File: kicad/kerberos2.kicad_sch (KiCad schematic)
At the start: 12 parts, among them J1 USB4125-GF-A_REVA2, J2 MIDI-in, J3 MIDI-thru, J4 MIDI-out, SW1 TL1105JAF160Q, U1 RP2040, U2 W9812G6KH-6, U3 T8Q144, U4 MX25L25645G

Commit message: first complete test version for Kerberos 2
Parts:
- removed D1, D2: LED, LED_THT:LED_D3.0mm, symbol Device:LED
- removed J1: USB4125-GF-A_REVA2, usb-c:GCT_USB4125-GF-A_REVA2, symbol USB4125-GF-A_REVA2:USB4125-GF-A_REVA2
- removed J2: MIDI-in, midi:CUI_SD-50BV, symbol SD-50BV:SD-50BV
- removed J3: MIDI-thru, midi:CUI_SD-50BV, symbol SD-50BV:SD-50BV
- removed J4: MIDI-out, midi:CUI_SD-50BV, symbol SD-50BV:SD-50BV
- removed SW1: TL1105JAF160Q, reset-button:SW_TL1105JAF160Q, symbol TL1105JAF160Q:TL1105JAF160Q
- removed U1: RP2040, rp2040:QFN40P700X700X90-57N, symbol RP2040:RP2040
- removed U2: W9812G6KH-6, Package_SO:TSOP-II-54_22.2x10.16mm_P0.8mm, symbol Memory_RAM:W9812G6KH-6
- removed U3: T8Q144, Package_QFP:LQFP-144_20x20mm_P0.5mm, symbol T8Q144:T8Q144
- added C1: 100n, Capacitor_SMD:C_0805_2012Metric, symbol Device:C
- added D1, D2: D_Schottky, Diode_SMD:D_SMA, symbol Device:D_Schottky
- added D3, D4: ~, LED_THT:LED_D3.0mm, symbol Device:LED
- added FB1: FerriteBead, Inductor_SMD:L_0805_2012Metric, symbol Device:FerriteBead
- added JP2: host-mode-supply, Connector_PinHeader_2.54mm:PinHeader_1x02_P2.54mm_Vertical, symbol Jumper:Jumper_2_Open
- added JP3: 3.3V+, Connector_PinHeader_2.54mm:PinHeader_1x02_P2.54mm_Vertical, symbol Jumper:Jumper_2_Open
- added JP4: 3.3V, Connector_PinHeader_2.54mm:PinHeader_1x02_P2.54mm_Vertical, symbol Jumper:Jumper_2_Open
- added JP5: 3.3V-, Connector_PinHeader_2.54mm:PinHeader_1x02_P2.54mm_Vertical, symbol Jumper:Jumper_2_Open
- added JP6: 1.2V+, Connector_PinHeader_2.54mm:PinHeader_1x02_P2.54mm_Vertical, symbol Jumper:Jumper_2_Open
- added JP7: 1.2V, Connector_PinHeader_2.54mm:PinHeader_1x02_P2.54mm_Vertical, symbol Jumper:Jumper_2_Open
- added JP8: 1.2V-, Connector_PinHeader_2.54mm:PinHeader_1x02_P2.54mm_Vertical, symbol Jumper:Jumper_2_Open
- added R1, R2: 5.1, Resistor_SMD:R_0805_2012Metric, symbol Device:R
- added R10, R11, R12, R13, R14, R15, R16, R17, R18, R19, R7, R8, R9: 22, Resistor_SMD:R_0805_2012Metric, symbol Device:R
- added R20, R21: 1k, Resistor_SMD:R_0805_2012Metric, symbol Device:R
- added R3, R4, R5, R6: 27, Resistor_SMD:R_0805_2012Metric, symbol Device:R
- added RN1, RN2, RN3, RN4, RN5: 33, resistor-network:16P8, symbol Device:R_Pack08
- added USB1: TYPEC-304J-BCP16, usb-c:USB-C-SMD_TYPEC-304J-BCP16, symbol TYPEC-304J-BCP16:TYPEC-304J-BCP16
- added X1: SX3M12.000M20F30TNN, oscillator:SX3M12.000M20F30TNN, symbol Oscillator:ASE-xxxMHz
- renumbered U4 to U1
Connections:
- net GND: now reaches JP1.1 (GND1)
- net GND: now also JP1.22 (GND3), JP1.A (GND2), JP1.Z (GND4), U1.4 (GND), C1.2, R1.1, R2.1, USB1.13 (GND), USB1.14 (GND), USB1.15 (GND), USB1.16 (GND), USB1.A1B12 (GND), USB1.B1A12 (GND), X1.2 (GND)
- net at JP1.10 (I/O2): now also RN2.7 (R7.1)
- net at JP1.11 (~{ROML}): now also RN2.6 (R6.1)
- net at JP1.12 (BA): now also RN1.6 (R6.1)
- net at JP1.13 (~{DMA}): now also RN1.7 (R7.1)
- net at JP1.14 (D7): now also RN5.9 (R8.2)
- net at JP1.15 (D6): now also RN5.10 (R7.2)
- net at JP1.16 (D5): now also RN5.11 (R6.2)
- net at JP1.17 (D4): now also RN5.12 (R5.2)
- net at JP1.18 (D3): now also RN5.13 (R4.2)
- net at JP1.19 (D2): now also RN5.14 (R3.2)
- net at JP1.2 (+5V1): now also JP1.3 (+5V2), D2.2 (A)
- net at JP1.20 (D1): now also RN5.15 (R2.2)
- net at JP1.21 (D0): now also RN5.16 (R1.2)
- net at JP1.4 (~{IRQ}): now also RN1.5 (R5.1)
- net at JP1.5 (R/W): now also RN1.4 (R4.1)
- net at JP1.6 (DOT-CLOCK): now also RN1.3 (R3.1)
- net at JP1.7 (I/O1): now also RN1.2 (R2.1)
- net at JP1.8 (~{GAME}): now also RN1.1 (R1.1)
- net at JP1.9 (~{EXROM}): now also RN2.8 (R8.1)
- net at JP1.B (~{ROMH}): now also RN2.5 (R5.1)
- net at JP1.C (~{RESET}): now also RN2.4 (R4.1)
- net at JP1.D (~{NMI}): now also RN2.3 (R3.1)
- net at JP1.E (S02): now also RN1.8 (R8.1)
- net at JP1.F (A15): now also RN4.9 (R8.2)
- net at JP1.H (A14): now also RN4.10 (R7.2)
- net at JP1.J (A13): now also RN4.11 (R6.2)
- net at JP1.K (A12): now also RN4.12 (R5.2)
- net at JP1.L (A11): now also RN4.13 (R4.2)
- net at JP1.M (A10): now also RN4.14 (R3.2)
- net at JP1.N (A9): now also RN4.15 (R2.2)
- net at JP1.P (A8): now also RN4.16 (R1.2)
- net at JP1.R (A7): now also RN3.9 (R8.2)
- net at JP1.S (A6): now also RN3.10 (R7.2)
- net at JP1.T (A5): now also RN3.11 (R6.2)
- net at JP1.U (A4): now also RN3.12 (R5.2)
- net at JP1.V (A3): now also RN3.13 (R4.2)
- net at JP1.W (A2): now also RN3.14 (R3.2)
- net at JP1.X (A1): now also RN3.15 (R2.2)
- net at JP1.Y (A0): now also RN3.16 (R1.2)
- net GW1NR FPGA/FLASH_CS: now reaches U1.1 (~{CS})
- net GW1NR FPGA/FLASH-SIO1: now reaches U1.2 (SO/SIO1)
- net GW1NR FPGA/FLASH-SIO2: now reaches U1.3 (~{WP}/SIO2)
- net GW1NR FPGA/FLASH-SIO0: now reaches U1.5 (SI/SIO0)
- net GW1NR FPGA/FLASH-SCLK: now reaches U1.6 (SCLK)
- net GW1NR FPGA/FLASH-SIO3: now reaches U1.7 (~{RESET}/SIO3)
- net +3.3V: now reaches U1.8 (VCC)
- net +3.3V: now also FB1.1, JP4.2 (B), JP5.2 (B), R20.1, R21.1
- new net: R3.1, R4.1, X1.3 (OUT)
- new net: C1.1, FB1.2, X1.4 (Vdd)
- new net: D1.2 (A), JP2.1 (A), USB1.A4B9 (VBUS), USB1.B4A9 (VBUS)
- new net: D3.2 (A), R20.2
- new net: R1.2, USB1.A5 (CC1)
- new net: R2.2, USB1.B5 (CC2)
- new net: D4.2 (A), R21.2
- new net +5V: D1.1 (K), D2.1 (K), JP2.2 (B)
- new net 1.2V: JP7.2 (B), JP8.2 (B)
- new net 1.2V power supply/Vout: JP6.1 (A), JP7.1 (A)
- new net 3.3V power supply/Vout: JP3.1 (A), JP4.1 (A)
- new net A0: RN3.1 (R1.1)
- new net A1: RN3.2 (R2.1)
- new net A10: RN4.3 (R3.1)
- new net A11: RN4.4 (R4.1)
- new net A12: RN4.5 (R5.1)
- new net A13: RN4.6 (R6.1)
- new net A14: RN4.7 (R7.1)
- new net A15: RN4.8 (R8.1)
- new net A2: RN3.3 (R3.1)
- new net A3: RN3.4 (R4.1)
- new net A4: RN3.5 (R5.1)
- new net A5: RN3.6 (R6.1)
- new net A6: RN3.7 (R7.1)
- new net A7: RN3.8 (R8.1)
- new net A8: RN4.1 (R1.1)
- new net A9: RN4.2 (R2.1)
- new net BA: RN1.11 (R6.2)
- new net D0: RN5.1 (R1.1)
- new net D1: RN5.2 (R2.1)
- new net D2: RN5.3 (R3.1)
- new net D3: RN5.4 (R4.1)
- new net D4: RN5.5 (R5.1)
- new net D5: RN5.6 (R6.1)
- new net D6: RN5.7 (R7.1)
- new net D7: RN5.8 (R8.1)
- new net DOT-CLK: RN1.14 (R3.2)
- new net GW1NR FPGA/CLK: R4.2
- new net GW1NR FPGA/DONE: R18.2
- new net GW1NR FPGA/JTAGSEL_N: R13.2
- new net GW1NR FPGA/MIDI-LED-in: D4.1 (K)
- new net GW1NR FPGA/MIDI-LED-out: D3.1 (K)
- new net GW1NR FPGA/RECONFIG_N: R19.2
- new net GW1NR FPGA/TCK: R14.2
- new net GW1NR FPGA/TDI: R17.2
- new net GW1NR FPGA/TDO: R16.2
- new net GW1NR FPGA/TMS: R15.2
- new net GW1NR FPGA/spare1: R7.2
- new net GW1NR FPGA/spare2: R8.2
- new net GW1NR FPGA/spare3: R9.2
- new net GW1NR FPGA/spare4: R10.2
- new net GW1NR FPGA/spare5: R11.2
- new net GW1NR FPGA/spare6: R12.2
- new net I/O1: RN1.15 (R2.2)
- new net I/O2: RN2.10 (R7.2)
- new net RP2040 microcontroller/DONE: R18.1
- new net RP2040 microcontroller/JTAGSEL_N: R13.1
- new net RP2040 microcontroller/RECONFIG_N: R19.1
- new net RP2040 microcontroller/TCK: R14.1
- new net RP2040 microcontroller/TDI: R17.1
- new net RP2040 microcontroller/TDO: R16.1
- new net RP2040 microcontroller/TMS: R15.1
- new net RP2040 microcontroller/USB_D+: R6.2
- new net RP2040 microcontroller/USB_D-: R5.2
- new net RP2040 microcontroller/XIN: R3.2
- new net RP2040 microcontroller/spare1: R7.1
- new net RP2040 microcontroller/spare2: R8.1
- new net RP2040 microcontroller/spare3: R9.1
- new net RP2040 microcontroller/spare4: R10.1
- new net RP2040 microcontroller/spare5: R11.1
- new net RP2040 microcontroller/spare6: R12.1
- new net R/W: RN1.13 (R4.2)
- new net S02: RN1.9 (R8.2)
- new net USB_D+: R6.1, USB1.A6 (DP1), USB1.B6 (DP2)
- new net USB_D-: R5.1, USB1.A7 (DN1), USB1.B7 (DN2)
- new net current sense/sense+: JP3.2 (B), JP6.2 (B)
- new net current sense/sense-: JP5.1 (A), JP8.1 (A)
- new net ~{DMA}: RN1.10 (R7.2)
- new net ~{EXROM}: RN2.9 (R8.2)
- new net ~{GAME}: RN1.16 (R1.2)
- new net ~{IRQ}: RN1.12 (R5.2)
- new net ~{NMI}: RN2.14 (R3.2)
- new net ~{RESET}: RN2.13 (R4.2)
- new net ~{ROMH}: RN2.12 (R5.2)
- new net ~{ROML}: RN2.11 (R6.2)
- no-connect marks 0 -> 1
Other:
- added sheet 1.2V power supply (power-supply.kicad_sch)
- added sheet 3.3V power supply (power-supply.kicad_sch)
- added sheet GW1NR FPGA (GW1NR.kicad_sch)
- added sheet MIDI (MIDI.kicad_sch)
- added sheet RP2040 microcontroller (RP2040.kicad_sch)
- added sheet current sense (current_sense.kicad_sch)
- moved on the sheet: JP1, U1

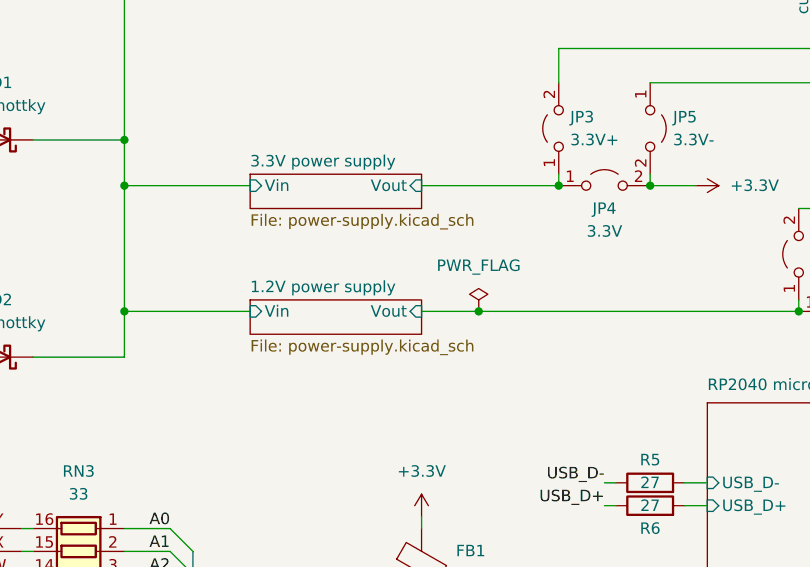
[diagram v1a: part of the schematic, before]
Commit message: added title to all circuit diagrams and sub-circuit diagrams, and PDF export
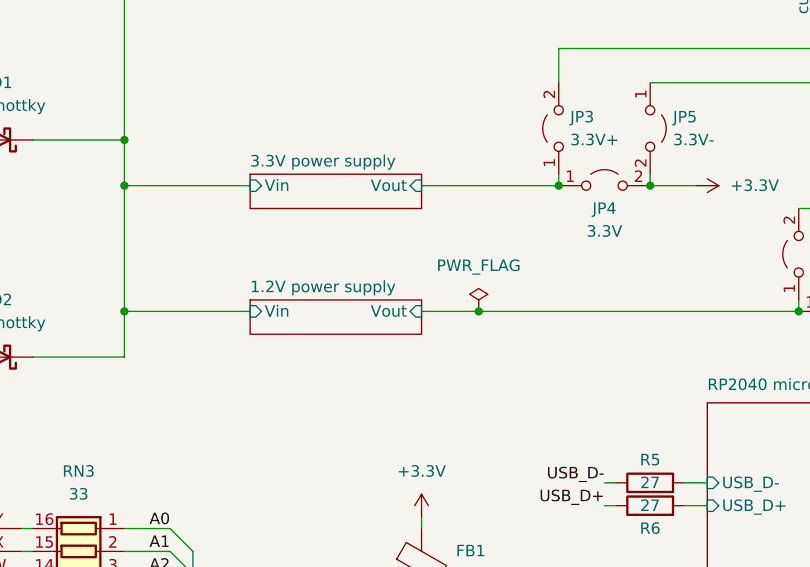
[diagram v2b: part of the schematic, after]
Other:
- title: (none) -> Kerberos 2
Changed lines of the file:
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@@
 (kicad_sch (version 20211123) (generator eeschema)
   (paper "A4")
+  (title_block
+    (title "Kerberos 2")
+  )
   (junction (at 53.34 67.31) (diameter 0) (color 0 0 0 0)
   )
@@
     )
     (property "Sheet file" "power-supply.kicad_sch" (id 1) (at 110.49 69.1646 0)
-      (effects (font (size 1.27 1.27)) (justify left top))
+      (effects (font (size 1.27 1.27)) (justify left top) hide)
     )
     (pin "Vin" input (at 110.49 66.04 180)
@@
     )
     (property "Sheet file" "power-supply.kicad_sch" (id 1) (at 110.49 55.1946 0)
-      (effects (font (size 1.27 1.27)) (justify left top))
+      (effects (font (size 1.27 1.27)) (justify left top) hide)
     )
     (pin "Vin" input (at 110.49 52.07 180)

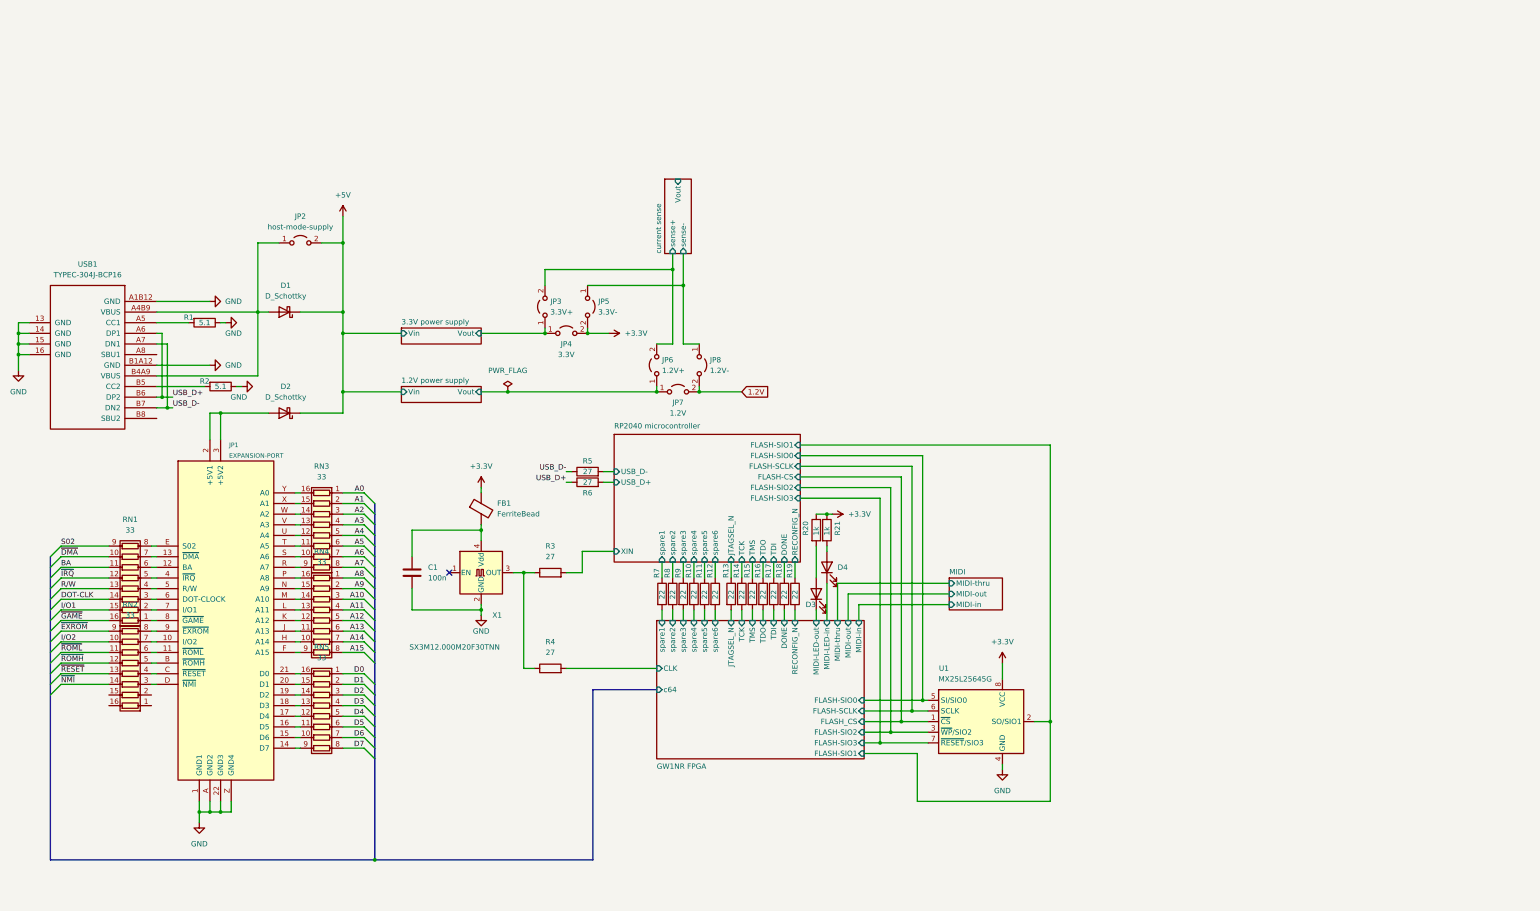
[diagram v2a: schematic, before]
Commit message: new flash, and IEC interface added
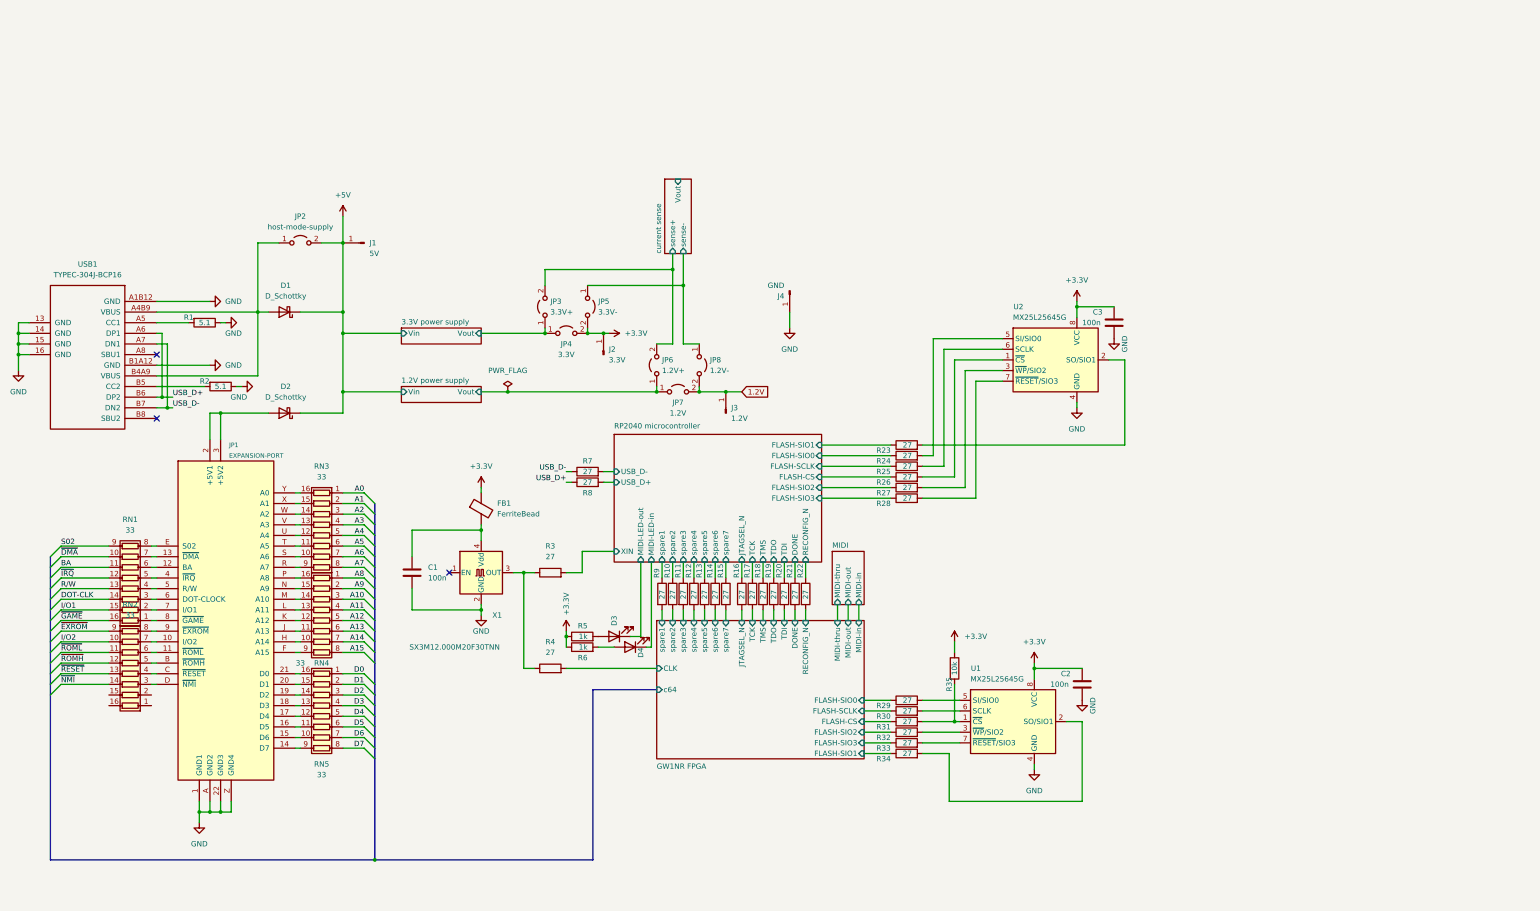
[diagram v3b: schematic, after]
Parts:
- added C2, C3: 100n, Capacitor_SMD:C_0805_2012Metric, symbol Device:C
- added J1: 5V, Connector_PinHeader_2.54mm:PinHeader_1x01_P2.54mm_Vertical, symbol Connector:Conn_01x01_Male
- added J2: 3.3V, Connector_PinHeader_2.54mm:PinHeader_1x01_P2.54mm_Vertical, symbol Connector:Conn_01x01_Male
- added J3: 1.2V, Connector_PinHeader_2.54mm:PinHeader_1x01_P2.54mm_Vertical, symbol Connector:Conn_01x01_Male
- added J4: GND, Connector_PinHeader_2.54mm:PinHeader_1x01_P2.54mm_Vertical, symbol Connector:Conn_01x01_Male
- added R15, R23, R24, R25, R26, R27, R28, R29, R30, R31, R32, R33, R34: 27, Resistor_SMD:R_0805_2012Metric, symbol Device:R
- added R35: 10k, Resistor_SMD:R_0805_2012Metric, symbol Device:R
- added U2: MX25L25645G, Package_SO:SOP-8_5.28x5.23mm_P1.27mm, symbol Memory_Flash:MX25R3235FM1xx0
- R10: renamed from R8; value 22 -> 27
- R11: renamed from R9; value 22 -> 27
- R12: renamed from R10; value 22 -> 27
- R13: renamed from R11; value 22 -> 27
- R14: renamed from R12; value 22 -> 27
- R16: renamed from R13; value 22 -> 27
- R17: renamed from R14; value 22 -> 27
- R18: renamed from R15; value 22 -> 27
- R19: renamed from R16; value 22 -> 27
- R20: renamed from R17; value 22 -> 27
- R21: renamed from R18; value 22 -> 27
- R22: renamed from R19; value 22 -> 27
- R9: renamed from R7; value 22 -> 27
- renumbered D4 to D3, D3 to D4, R21 to R5, R20 to R6, R5 to R7, R6 to R8
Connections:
- net +3.3V: now also C2.1, C3.1, J2.1 (Pin_1), R35.1, U2.8 (VCC)
- net +5V: now also J1.1 (Pin_1)
- net 1.2V: now also J3.1 (Pin_1)
- net GND: now also C2.2, C3.2, J4.1 (Pin_1), U2.4 (GND)
- net GW1NR FPGA/FLASH-SCLK: now also R30.1; no longer U1.6 (SCLK)
- net GW1NR FPGA/FLASH-SIO0: now also R29.1; no longer U1.5 (SI/SIO0)
- net GW1NR FPGA/FLASH-SIO1: now also R34.1; no longer U1.2 (SO/SIO1)
- net GW1NR FPGA/FLASH-SIO2: now also R32.1; no longer U1.3 (~{WP}/SIO2)
- net GW1NR FPGA/FLASH-SIO3: now also R33.1; no longer U1.7 (~{RESET}/SIO3)
- net GW1NR FPGA/FLASH_CS: no longer names the net of U1.1 (~{CS})
- net GW1NR FPGA/FLASH_CS: now also R31.2, R35.2
- net GW1NR FPGA/MIDI-LED-in renamed RP2040 microcontroller/MIDI-LED-out
- net GW1NR FPGA/MIDI-LED-out renamed RP2040 microcontroller/MIDI-LED-in
- new net: R34.2, U1.2 (SO/SIO1)
- new net: R26.2, U2.1 (~{CS})
- new net: R30.2, U1.6 (SCLK)
- new net: R25.2, U2.6 (SCLK)
- new net: R23.2, U2.2 (SO/SIO1)
- new net: R27.2, U2.3 (~{WP}/SIO2)
- new net: R24.2, U2.5 (SI/SIO0)
- new net: R28.2, U2.7 (~{RESET}/SIO3)
- new net: R32.2, U1.3 (~{WP}/SIO2)
- new net: R33.2, U1.7 (~{RESET}/SIO3)
- new net: R29.2, U1.5 (SI/SIO0)
- new net GW1NR FPGA/FLASH-CS: R31.1
- new net GW1NR FPGA/spare7: R15.2
- new net RP2040 microcontroller/FLASH-CS: R26.1
- new net RP2040 microcontroller/FLASH-SCLK: R25.1
- new net RP2040 microcontroller/FLASH-SIO0: R24.1
- new net RP2040 microcontroller/FLASH-SIO1: R23.1
- new net RP2040 microcontroller/FLASH-SIO2: R27.1
- new net RP2040 microcontroller/FLASH-SIO3: R28.1
- new net RP2040 microcontroller/spare7: R15.1
- no-connect marks 1 -> 3
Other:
- sheet GW1NR FPGA ports: added FLASH-CS, spare7; removed FLASH_CS, MIDI-LED-in, MIDI-LED-out
- sheet RP2040 microcontroller ports: added MIDI-LED-in, MIDI-LED-out, spare7; removed none
- moved on the sheet: D3, D4, R16, R17, R18, R19, R20, R21, R22, R5, R6, U1
